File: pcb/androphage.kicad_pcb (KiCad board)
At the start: 2 copper layers, 150 x 113 mm, 56 parts, among them J1 VIK_OUT_PMWL, J2 VIK_OUT_INTC, J3 VIK_IN, J4 VIK_OUT_PMWR, J5 Conn_01x02, U1 nice_nano, U2 MCP23017_SO, U3 MCP23017_SO

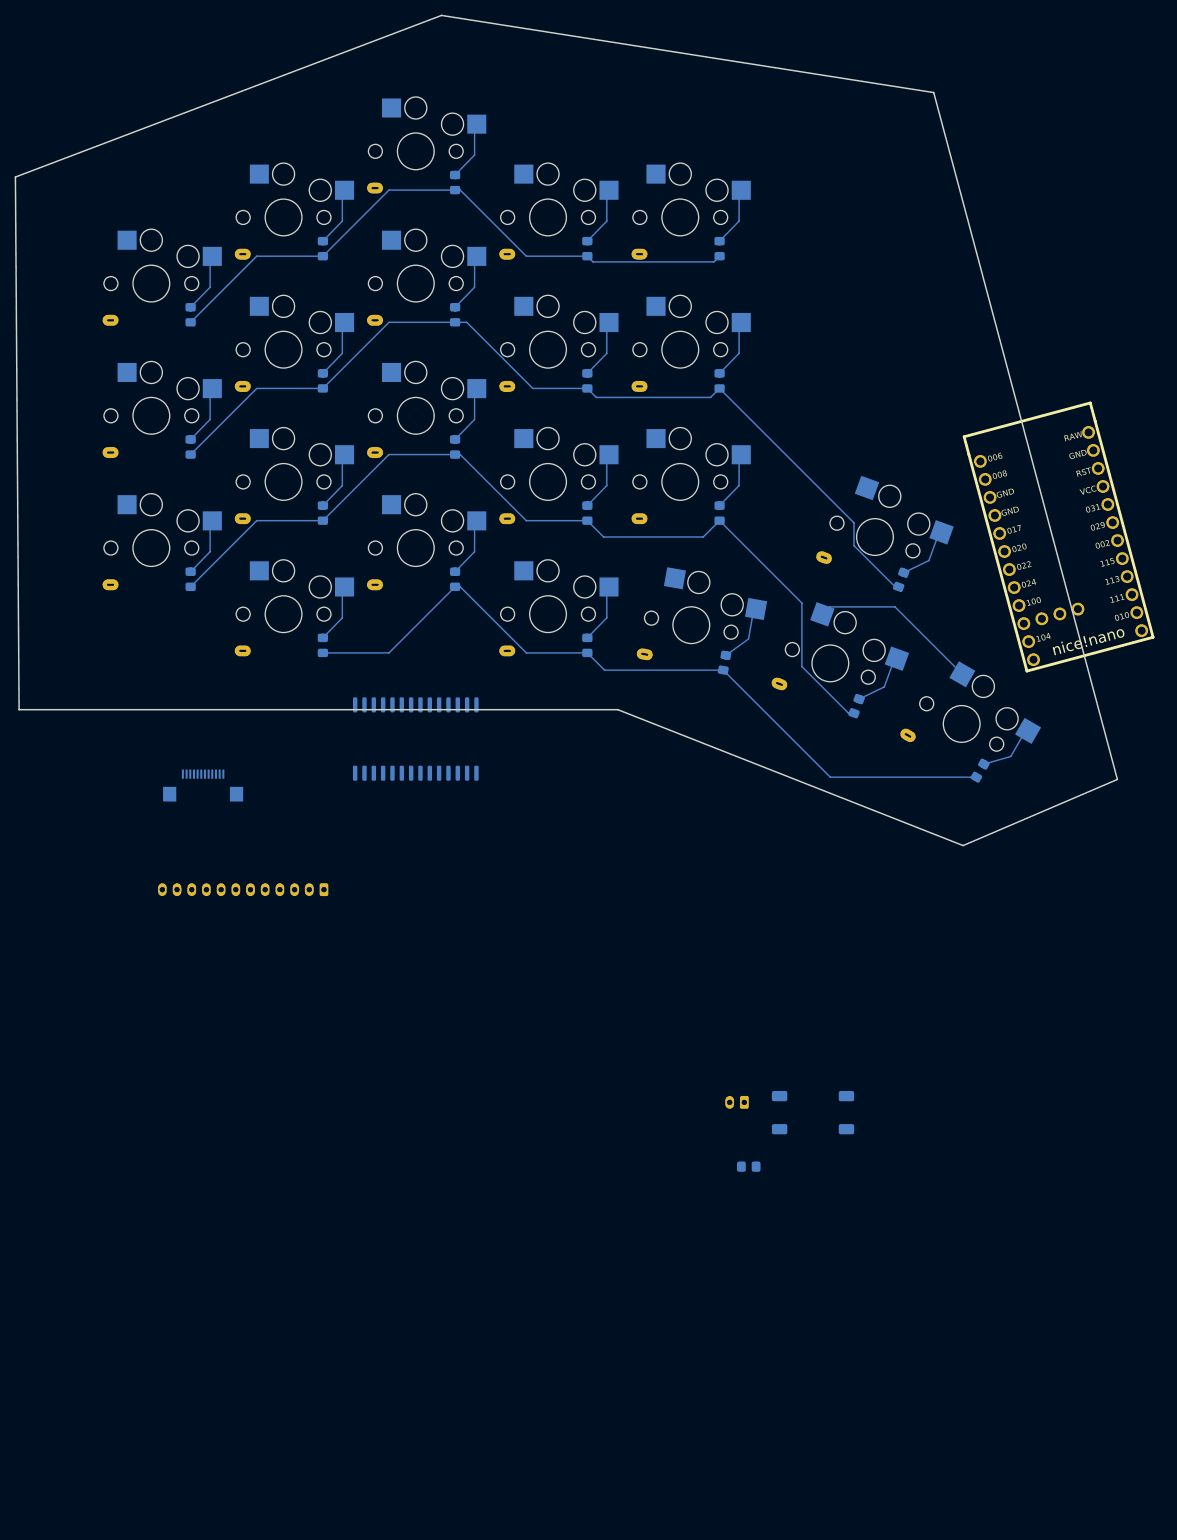
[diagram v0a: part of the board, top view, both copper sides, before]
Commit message: Create VIK hat for Seeed Xiao nRF.
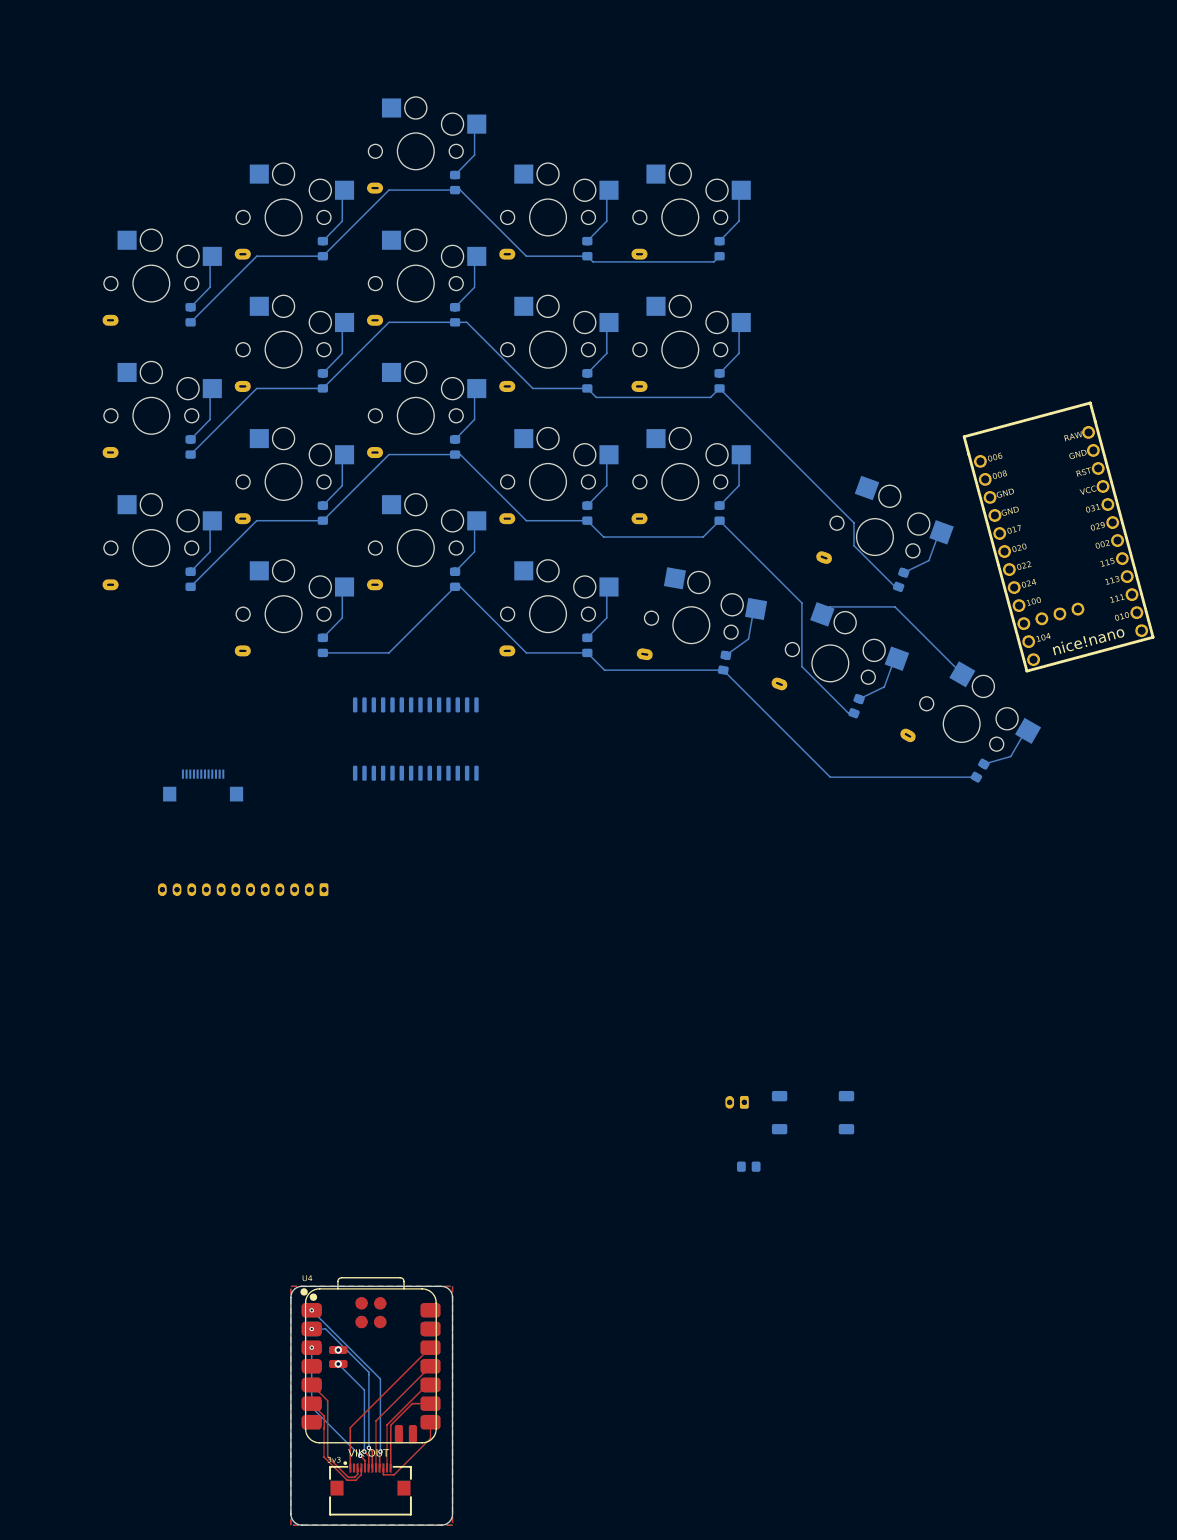
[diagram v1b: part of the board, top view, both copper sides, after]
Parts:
- added J6: VIK_OUT, vik:vik-keyboard-connector-horizontal, F.Cu at (29.8, 181.3)
- added REF**: vik-logo-medium, vik:vik-logo-medium, B.Cu at (30.0, 164.0)
- added U4: XIAO-nRF52840-SMD, footprints:XIAO-nRF52840-SMD, F.Cu at (29.9, 165.4)
- R1: value 8K -> 8K2
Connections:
- J2 pad 9: /Left/GP1 -> /Left/PWRSAV
- U1 pad 14: /Left/GP1 -> /Left/PWRSAV
- U3 pad 5: unconnected-(U3-GPB4-Pad5) -> /Left/PWRSAV
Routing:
- net /Xiao_VIK_Hat/INT_PMWR: track 0.00 -> 25.4 mm, vias 0 -> 2
- net /Xiao_VIK_Hat/INT_PMWL: track 0.00 -> 23.4 mm, vias 0 -> 2
- net /Xiao_VIK_Hat/3V3: track 0.00 -> 20.9 mm
- net /Xiao_VIK_Hat/RGB_DO: track 0.00 -> 19.4 mm, vias 0 -> 2
- net /Xiao_VIK_Hat/SDA: track 0.00 -> 16.9 mm
- net /Xiao_VIK_Hat/MOSI: track 0.00 -> 16.9 mm
- net /Xiao_VIK_Hat/VBATT: track 0.00 -> 15.9 mm, vias 0 -> 2
- net /Xiao_VIK_Hat/SCL: track 0.00 -> 15.6 mm
- net /Xiao_VIK_Hat/MISO: track 0.00 -> 14.0 mm
- net /Xiao_VIK_Hat/SCK: track 0.00 -> 12.5 mm
- net /Xiao_VIK_Hat/CS: track 0.00 -> 11.6 mm
- net /Xiao_VIK_Hat/GND: vias 0 -> 1
- added copper zone on B.Cu, net /Xiao_VIK_Hat/GND
- added copper zone on F.Cu, net /Xiao_VIK_Hat/GND
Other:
- board size 150 x 113 mm -> 22 x 32.5 mm

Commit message: Tentatively finish PCB design.
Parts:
- removed J1: VIK_OUT_PMWL, vik:vik-keyboard-connector-horizontal
- removed J2: VIK_OUT_INTC, Connector_JST:JST_PH_S12B-PH-K_1x12_P2.00mm_Horizontal
- removed J3: VIK_IN, Connector_JST:JST_PH_S12B-PH-K_1x12_P2.00mm_Horizontal
- removed J4: VIK_OUT_PMWR, vik:vik-keyboard-connector-horizontal
- removed R1: 8K2, Resistor_SMD:R_0805_2012Metric_Pad1.20x1.40mm_HandSolder
- removed R2, R3: 8K, Resistor_SMD:R_0805_2012Metric_Pad1.20x1.40mm_HandSolder
- removed REF**: vik-logo-medium, vik:vik-logo-medium
- removed SW_RST1: SW_Push, Button_Switch_SMD:SW_Push_1P1T_NO_E-Switch_TL3301NxxxxxG
- removed U1: nice_nano, footprints:nice_nano
- removed U2, U3: MCP23017_SO, Package_SO:SOIC-28W_7.5x17.9mm_P1.27mm
- removed U4: XIAO-nRF52840-SMD, footprints:XIAO-nRF52840-SMD
- added D1: SK6812MINI, LED_SMD:LED_SK6812MINI_PLCC4_3.5x3.5mm_P1.75mm, F.Cu at (29.2, 67.0)
- added D2: SK6812MINI, LED_SMD:LED_SK6812MINI_PLCC4_3.5x3.5mm_P1.75mm, F.Cu at (33.8, 67.0)
- added D3: SK6812MINI, LED_SMD:LED_SK6812MINI_PLCC4_3.5x3.5mm_P1.75mm, F.Cu at (38.2, 67.0)
- added D4: SK6812MINI, LED_SMD:LED_SK6812MINI_PLCC4_3.5x3.5mm_P1.75mm, F.Cu at (42.8, 67.0)
- added D5: SK6812MINI, LED_SMD:LED_SK6812MINI_PLCC4_3.5x3.5mm_P1.75mm, F.Cu at (242.8, 67.0)
- added D6: SK6812MINI, LED_SMD:LED_SK6812MINI_PLCC4_3.5x3.5mm_P1.75mm, F.Cu at (238.2, 67.0)
- added D7: SK6812MINI, LED_SMD:LED_SK6812MINI_PLCC4_3.5x3.5mm_P1.75mm, F.Cu at (233.8, 67.0)
- added D8: SK6812MINI, LED_SMD:LED_SK6812MINI_PLCC4_3.5x3.5mm_P1.75mm, F.Cu at (229.2, 67.0)
- J5: value Conn_01x02 -> Conn_02x08; footprint Connector_JST:JST_PH_S2B-PH-K_1x02_P2.00mm_Horizontal -> Connector_PinHeader_2.54mm:PinHeader_2x08_P2.54mm_Vertical
- J6: value VIK_OUT -> Conn_02x08; footprint vik:vik-keyboard-connector-horizontal -> Connector_PinHeader_2.54mm:PinHeader_2x08_P2.54mm_Vertical
- moved J6 265.0 mm to (217.9, -5.50), turned to -90 degrees
- moved J5 137.6 mm to (53.9, -5.50), turned to -90 degrees
- moved SWR15 0.58 mm to (173.3, 52.9)
- moved SWR35 0.45 mm to (161.8, 78.1)
- moved SWR25 0.38 mm to (179.5, 69.8)
- moved SWL15 0.37 mm to (98.6, 52.8)
- moved SWL34 0.21 mm to (73.5, 64.7)
- moved SWR34 0.21 mm to (198.5, 64.7)
- moved SWL35 0.11 mm to (110.3, 78.0)
- moved SWL25 0.09 mm to (92.5, 69.8)
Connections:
- J5 pad 1: /Left/VBATT -> /Left_Switches/VBATT
- J5 pad 2: /Left/GND -> /Left_Switches/3V3
- J6 pad 1: /Xiao_VIK_Hat/3V3 -> /Right_Switches/VBATT
- J6 pad 10: /Xiao_VIK_Hat/CS -> /Right_Switches/C3
- J6 pad 11: /Xiao_VIK_Hat/MISO -> /Right_Switches/R2
- J6 pad 12: /Xiao_VIK_Hat/SCK -> /Right_Switches/C4
- J6 pad 13: (no net) -> /Right_Switches/R3
- J6 pad 14: (no net) -> /Right_Switches/C5
- J6 pad 2: /Xiao_VIK_Hat/GND -> /Right_Switches/3V3
- J6 pad 3: /Xiao_VIK_Hat/SDA -> /Right_Switches/RGB_DO
- J6 pad 4: /Xiao_VIK_Hat/SCL -> /Right_Switches/C0
- J6 pad 5: /Xiao_VIK_Hat/RGB_DO -> /Right_Switches/GP1_KB
- J6 pad 6: /Xiao_VIK_Hat/VBATT -> /Right_Switches/C1
- J6 pad 7: /Xiao_VIK_Hat/INT_PMWL -> /Right_Switches/R0
- J6 pad 8: /Xiao_VIK_Hat/MOSI -> /Right_Switches/C2
- J6 pad 9: /Xiao_VIK_Hat/INT_PMWR -> /Right_Switches/R1
- SWL00 pad 1: /Left/C0 -> /Left_Switches/C0
- SWL00 pad 2: /Left/R0 -> /Left_Switches/R0
- SWL01 pad 1: /Left/C1 -> /Left_Switches/C1
- SWL01 pad 2: /Left/R0 -> /Left_Switches/R0
- SWL02 pad 1: /Left/C2 -> /Left_Switches/C2
- SWL02 pad 2: /Left/R0 -> /Left_Switches/R0
- SWL03 pad 1: /Left/C3 -> /Left_Switches/C3
- SWL03 pad 2: /Left/R0 -> /Left_Switches/R0
- SWL04 pad 1: /Left/C4 -> /Left_Switches/C4
- SWL04 pad 2: /Left/R0 -> /Left_Switches/R0
- SWL10 pad 1: /Left/C0 -> /Left_Switches/C0
- SWL10 pad 2: /Left/R1 -> /Left_Switches/R1
- SWL11 pad 1: /Left/C1 -> /Left_Switches/C1
- SWL11 pad 2: /Left/R1 -> /Left_Switches/R1
- SWL12 pad 1: /Left/C2 -> /Left_Switches/C2
- SWL12 pad 2: /Left/R1 -> /Left_Switches/R1
- SWL13 pad 1: /Left/C3 -> /Left_Switches/C3
- SWL13 pad 2: /Left/R1 -> /Left_Switches/R1
- SWL14 pad 1: /Left/C4 -> /Left_Switches/C4
- SWL14 pad 2: /Left/R1 -> /Left_Switches/R1
- SWL15 pad 1: /Left/C5 -> /Left_Switches/C5
- SWL15 pad 2: /Left/R1 -> /Left_Switches/R1
- SWL20 pad 1: /Left/C0 -> /Left_Switches/C0
- SWL20 pad 2: /Left/R2 -> /Left_Switches/R2
- SWL21 pad 1: /Left/C1 -> /Left_Switches/C1
- SWL21 pad 2: /Left/R2 -> /Left_Switches/R2
- SWL22 pad 1: /Left/C2 -> /Left_Switches/C2
- SWL22 pad 2: /Left/R2 -> /Left_Switches/R2
- SWL23 pad 1: /Left/C3 -> /Left_Switches/C3
- SWL23 pad 2: /Left/R2 -> /Left_Switches/R2
- SWL24 pad 1: /Left/C4 -> /Left_Switches/C4
- SWL24 pad 2: /Left/R2 -> /Left_Switches/R2
- SWL25 pad 1: /Left/C5 -> /Left_Switches/C5
- SWL25 pad 2: /Left/R2 -> /Left_Switches/R2
- SWL31 pad 1: /Left/C1 -> /Left_Switches/C1
- SWL31 pad 2: /Left/R3 -> /Left_Switches/R3
- SWL32 pad 1: /Left/C2 -> /Left_Switches/C2
- SWL32 pad 2: /Left/R3 -> /Left_Switches/R3
- SWL33 pad 1: /Left/C3 -> /Left_Switches/C3
- SWL33 pad 2: /Left/R3 -> /Left_Switches/R3
- SWL34 pad 1: /Left/C4 -> /Left_Switches/C4
- SWL34 pad 2: /Left/R3 -> /Left_Switches/R3
- SWL35 pad 1: /Left/C5 -> /Left_Switches/C5
- SWL35 pad 2: /Left/R3 -> /Left_Switches/R3
- SWR00 pad 1: /Right/C0 -> /Right_Switches/C0
- SWR00 pad 2: /Right/R0 -> /Right_Switches/R0
- SWR01 pad 1: /Right/C1 -> /Right_Switches/C1
- SWR01 pad 2: /Right/R0 -> /Right_Switches/R0
- SWR02 pad 1: /Right/C2 -> /Right_Switches/C2
- SWR02 pad 2: /Right/R0 -> /Right_Switches/R0
- SWR03 pad 1: /Right/C3 -> /Right_Switches/C3
- SWR03 pad 2: /Right/R0 -> /Right_Switches/R0
- SWR04 pad 1: /Right/C4 -> /Right_Switches/C4
- SWR04 pad 2: /Right/R0 -> /Right_Switches/R0
- SWR10 pad 1: /Right/C0 -> /Right_Switches/C0
- SWR10 pad 2: /Right/R1 -> /Right_Switches/R1
- SWR11 pad 1: /Right/C1 -> /Right_Switches/C1
- SWR11 pad 2: /Right/R1 -> /Right_Switches/R1
- SWR12 pad 1: /Right/C2 -> /Right_Switches/C2
- SWR12 pad 2: /Right/R1 -> /Right_Switches/R1
- SWR13 pad 1: /Right/C3 -> /Right_Switches/C3
- SWR13 pad 2: /Right/R1 -> /Right_Switches/R1
- SWR14 pad 1: /Right/C4 -> /Right_Switches/C4
- SWR14 pad 2: /Right/R1 -> /Right_Switches/R1
- SWR15 pad 1: /Right/C5 -> /Right_Switches/C5
- SWR15 pad 2: /Right/R1 -> /Right_Switches/R1
- SWR20 pad 1: /Right/C0 -> /Right_Switches/C0
- SWR20 pad 2: /Right/R2 -> /Right_Switches/R2
- SWR21 pad 1: /Right/C1 -> /Right_Switches/C1
- SWR21 pad 2: /Right/R2 -> /Right_Switches/R2
- SWR22 pad 1: /Right/C2 -> /Right_Switches/C2
- SWR22 pad 2: /Right/R2 -> /Right_Switches/R2
- SWR23 pad 1: /Right/C3 -> /Right_Switches/C3
- SWR23 pad 2: /Right/R2 -> /Right_Switches/R2
- SWR24 pad 1: /Right/C4 -> /Right_Switches/C4
- SWR24 pad 2: /Right/R2 -> /Right_Switches/R2
- SWR25 pad 1: /Right/C5 -> /Right_Switches/C5
- SWR25 pad 2: /Right/R2 -> /Right_Switches/R2
- SWR31 pad 1: /Right/C1 -> /Right_Switches/C1
- SWR31 pad 2: /Right/R3 -> /Right_Switches/R3
- SWR32 pad 1: /Right/C2 -> /Right_Switches/C2
- SWR32 pad 2: /Right/R3 -> /Right_Switches/R3
- SWR33 pad 1: /Right/C3 -> /Right_Switches/C3
- SWR33 pad 2: /Right/R3 -> /Right_Switches/R3
- SWR34 pad 1: /Right/C4 -> /Right_Switches/C4
- SWR34 pad 2: /Right/R3 -> /Right_Switches/R3
- SWR35 pad 1: /Right/C5 -> /Right_Switches/C5
- SWR35 pad 2: /Right/R3 -> /Right_Switches/R3
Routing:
- net /Left_Switches/R3: track 0.00 -> 277.9 mm
- net /Left_Switches/R2: track 0.00 -> 271.6 mm
- net /Right_Switches/R3: track 0.00 -> 268.8 mm
- net /Right_Switches/R2: track 0.00 -> 262.1 mm
- net /Left_Switches/R1: track 0.00 -> 253.9 mm
- net /Right_Switches/R1: track 0.00 -> 242.1 mm
- net /Right_Switches/R0: track 0.00 -> 183.5 mm
- net /Left_Switches/R0: track 0.00 -> 167.5 mm
- net /Right_Switches/VBATT: track 0.00 -> 147.7 mm
- net /Left_Switches/VBATT: track 0.00 -> 146.7 mm
- net /Left_Switches/RGB_DO: track 0.00 -> 130.2 mm
- net /Left/R1: track 121.6 -> 0.00 mm
- net /Left/R2: track 119.3 -> 0.00 mm
- net /Right_Switches/C5: track 0.00 -> 116.9 mm
- net /Left_Switches/C0: track 0.00 -> 116.7 mm
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- added copper zone on B.Cu, net /Left_Switches/GND
- added copper zone on F.Cu, net /Left_Switches/GND
- added copper zone on B.Cu, net /Right_Switches/GND
- added copper zone on F.Cu, net /Right_Switches/GND
- removed copper zone on B.Cu, net /Xiao_VIK_Hat/GND
- removed copper zone on F.Cu, net /Xiao_VIK_Hat/GND
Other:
- board size 22 x 32.5 mm -> 300 x 108.2 mm
